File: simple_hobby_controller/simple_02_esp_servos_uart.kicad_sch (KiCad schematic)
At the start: 19 parts, among them J10 WRIST SERVO, J11 PI UART - 2.54 mm HEADER, J7 ESP32-PICO-KIT V4.1, J8 MAIN SWING SERVO, J9 ELBOW SERVO

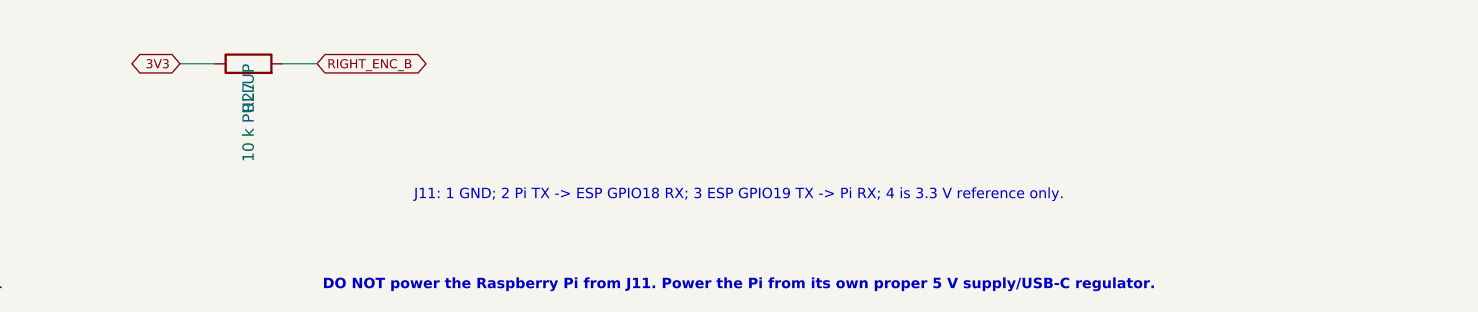
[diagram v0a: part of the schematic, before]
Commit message: Add onboard shared 5V buck rail
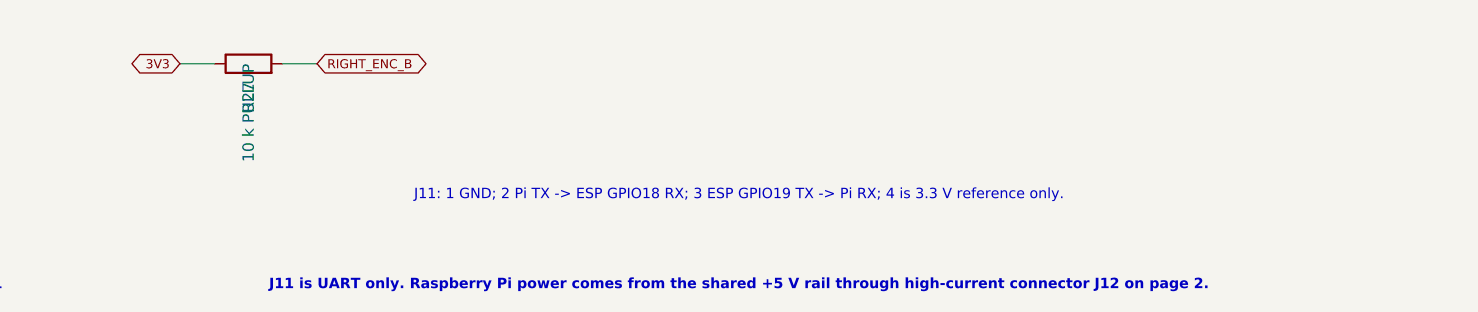
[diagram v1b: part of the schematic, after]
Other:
- note added: "J11 is UART only. Raspberry Pi power comes from the shared +5 V rail through high-current connector J12 on page 2."
- note removed: "DO NOT power the Raspberry Pi from J11. Power the Pi from its own proper 5 V supply/USB-C regulator."
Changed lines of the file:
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@@
 		(instances
 			(project "pickleball_robot_simple"
-				(path "/c5a03a22-6458-40bc-9f85-a426ca2b5b75/77d8af3d-e1ce-4b27-91ae-0678f28405f6"
+				(path "/6df0ee1a-c63b-4ad4-8bcd-d4ab373e7ba7/0037a72a-c13a-44ed-98be-bca8f0dd50a2"
 					(reference "J7")
 					(unit 1)
@@
 		(instances
 			(project "pickleball_robot_simple"
-				(path "/c5a03a22-6458-40bc-9f85-a426ca2b5b75/77d8af3d-e1ce-4b27-91ae-0678f28405f6"
+				(path "/6df0ee1a-c63b-4ad4-8bcd-d4ab373e7ba7/0037a72a-c13a-44ed-98be-bca8f0dd50a2"
 					(reference "J8")
 					(unit 1)
@@
 		(instances
 			(project "pickleball_robot_simple"
-				(path "/c5a03a22-6458-40bc-9f85-a426ca2b5b75/77d8af3d-e1ce-4b27-91ae-0678f28405f6"
+				(path "/6df0ee1a-c63b-4ad4-8bcd-d4ab373e7ba7/0037a72a-c13a-44ed-98be-bca8f0dd50a2"
 					(reference "R10")
 					(unit 1)
@@
 		(instances
 			(project "pickleball_robot_simple"
-				(path "/c5a03a22-6458-40bc-9f85-a426ca2b5b75/77d8af3d-e1ce-4b27-91ae-0678f28405f6"
+				(path "/6df0ee1a-c63b-4ad4-8bcd-d4ab373e7ba7/0037a72a-c13a-44ed-98be-bca8f0dd50a2"
 					(reference "R13")
 					(unit 1)
@@
 		(instances
 			(project "pickleball_robot_simple"
-				(path "/c5a03a22-6458-40bc-9f85-a426ca2b5b75/77d8af3d-e1ce-4b27-91ae-0678f28405f6"
+				(path "/6df0ee1a-c63b-4ad4-8bcd-d4ab373e7ba7/0037a72a-c13a-44ed-98be-bca8f0dd50a2"
 					(reference "J9")
 					(unit 1)
@@
 		(instances
 			(project "pickleball_robot_simple"
-				(path "/c5a03a22-6458-40bc-9f85-a426ca2b5b75/77d8af3d-e1ce-4b27-91ae-0678f28405f6"
+				(path "/6df0ee1a-c63b-4ad4-8bcd-d4ab373e7ba7/0037a72a-c13a-44ed-98be-bca8f0dd50a2"
 					(reference "R11")
 					(unit 1)
@@
 		(instances
 			(project "pickleball_robot_simple"
-				(path "/c5a03a22-6458-40bc-9f85-a426ca2b5b75/77d8af3d-e1ce-4b27-91ae-0678f28405f6"
+				(path "/6df0ee1a-c63b-4ad4-8bcd-d4ab373e7ba7/0037a72a-c13a-44ed-98be-bca8f0dd50a2"
 					(reference "R14")
 					(unit 1)
@@
 		(instances
 			(project "pickleball_robot_simple"
-				(path "/c5a03a22-6458-40bc-9f85-a426ca2b5b75/77d8af3d-e1ce-4b27-91ae-0678f28405f6"
+				(path "/6df0ee1a-c63b-4ad4-8bcd-d4ab373e7ba7/0037a72a-c13a-44ed-98be-bca8f0dd50a2"
 					(reference "J10")
 					(unit 1)
@@
 		(instances
 			(project "pickleball_robot_simple"
-				(path "/c5a03a22-6458-40bc-9f85-a426ca2b5b75/77d8af3d-e1ce-4b27-91ae-0678f28405f6"
+				(path "/6df0ee1a-c63b-4ad4-8bcd-d4ab373e7ba7/0037a72a-c13a-44ed-98be-bca8f0dd50a2"
 					(reference "R12")
 					(unit 1)
@@
 		(instances
 			(project "pickleball_robot_simple"
-				(path "/c5a03a22-6458-40bc-9f85-a426ca2b5b75/77d8af3d-e1ce-4b27-91ae-0678f28405f6"
+				(path "/6df0ee1a-c63b-4ad4-8bcd-d4ab373e7ba7/0037a72a-c13a-44ed-98be-bca8f0dd50a2"
 					(reference "R15")
 					(unit 1)
@@
 		(instances
 			(project "pickleball_robot_simple"
-				(path "/c5a03a22-6458-40bc-9f85-a426ca2b5b75/77d8af3d-e1ce-4b27-91ae-0678f28405f6"
+				(path "/6df0ee1a-c63b-4ad4-8bcd-d4ab373e7ba7/0037a72a-c13a-44ed-98be-bca8f0dd50a2"
 					(reference "R20")
 					(unit 1)
@@
 		(instances
 			(project "pickleball_robot_simple"
-				(path "/c5a03a22-6458-40bc-9f85-a426ca2b5b75/77d8af3d-e1ce-4b27-91ae-0678f28405f6"
+				(path "/6df0ee1a-c63b-4ad4-8bcd-d4ab373e7ba7/0037a72a-c13a-44ed-98be-bca8f0dd50a2"
 					(reference "R24")
 					(unit 1)
@@
 		(instances
 			(project "pickleball_robot_simple"
-				(path "/c5a03a22-6458-40bc-9f85-a426ca2b5b75/77d8af3d-e1ce-4b27-91ae-0678f28405f6"
+				(path "/6df0ee1a-c63b-4ad4-8bcd-d4ab373e7ba7/0037a72a-c13a-44ed-98be-bca8f0dd50a2"
 					(reference "R21")
 					(unit 1)
@@
 		(instances
 			(project "pickleball_robot_simple"
-				(path "/c5a03a22-6458-40bc-9f85-a426ca2b5b75/77d8af3d-e1ce-4b27-91ae-0678f28405f6"
+				(path "/6df0ee1a-c63b-4ad4-8bcd-d4ab373e7ba7/0037a72a-c13a-44ed-98be-bca8f0dd50a2"
 					(reference "R25")
 					(unit 1)
@@
 		(instances
 			(project "pickleball_robot_simple"
-				(path "/c5a03a22-6458-40bc-9f85-a426ca2b5b75/77d8af3d-e1ce-4b27-91ae-0678f28405f6"
+				(path "/6df0ee1a-c63b-4ad4-8bcd-d4ab373e7ba7/0037a72a-c13a-44ed-98be-bca8f0dd50a2"
 					(reference "R22")
 					(unit 1)
@@
 		(instances
 			(project "pickleball_robot_simple"
-				(path "/c5a03a22-6458-40bc-9f85-a426ca2b5b75/77d8af3d-e1ce-4b27-91ae-0678f28405f6"
+				(path "/6df0ee1a-c63b-4ad4-8bcd-d4ab373e7ba7/0037a72a-c13a-44ed-98be-bca8f0dd50a2"
 					(reference "R26")
 					(unit 1)
@@
 		(instances
 			(project "pickleball_robot_simple"
-				(path "/c5a03a22-6458-40bc-9f85-a426ca2b5b75/77d8af3d-e1ce-4b27-91ae-0678f28405f6"
+				(path "/6df0ee1a-c63b-4ad4-8bcd-d4ab373e7ba7/0037a72a-c13a-44ed-98be-bca8f0dd50a2"
 					(reference "R23")
 					(unit 1)
@@
 		(instances
 			(project "pickleball_robot_simple"
-				(path "/c5a03a22-6458-40bc-9f85-a426ca2b5b75/77d8af3d-e1ce-4b27-91ae-0678f28405f6"
+				(path "/6df0ee1a-c63b-4ad4-8bcd-d4ab373e7ba7/0037a72a-c13a-44ed-98be-bca8f0dd50a2"
 					(reference "R27")
 					(unit 1)
@@
 		(instances
 			(project "pickleball_robot_simple"
-				(path "/c5a03a22-6458-40bc-9f85-a426ca2b5b75/77d8af3d-e1ce-4b27-91ae-0678f28405f6"
+				(path "/6df0ee1a-c63b-4ad4-8bcd-d4ab373e7ba7/0037a72a-c13a-44ed-98be-bca8f0dd50a2"
 					(reference "J11")
 					(unit 1)
@@
 		)
 	)
-	(text "DO NOT power the Raspberry Pi from J11. Power the Pi from its own proper 5 V supply/USB-C regulator."
+	(text "J11 is UART only. Raspberry Pi power comes from the shared +5 V rail through high-current connector J12 on page 2."
 		(exclude_from_sim no)
 		(at 245 285 0.0000)
@@
 	)
 	(sheet_instances
-		(path "/c5a03a22-6458-40bc-9f85-a426ca2b5b75/77d8af3d-e1ce-4b27-91ae-0678f28405f6"
+		(path "/6df0ee1a-c63b-4ad4-8bcd-d4ab373e7ba7/0037a72a-c13a-44ed-98be-bca8f0dd50a2"
 			(page "3")
 		)
